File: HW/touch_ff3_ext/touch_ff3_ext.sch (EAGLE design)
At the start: 6 parts, among them M1 SMALL_SERVO, P8 DF9-31P, Q1 MOSFET-NCHANNELAO3404A, X3 DF9-31S

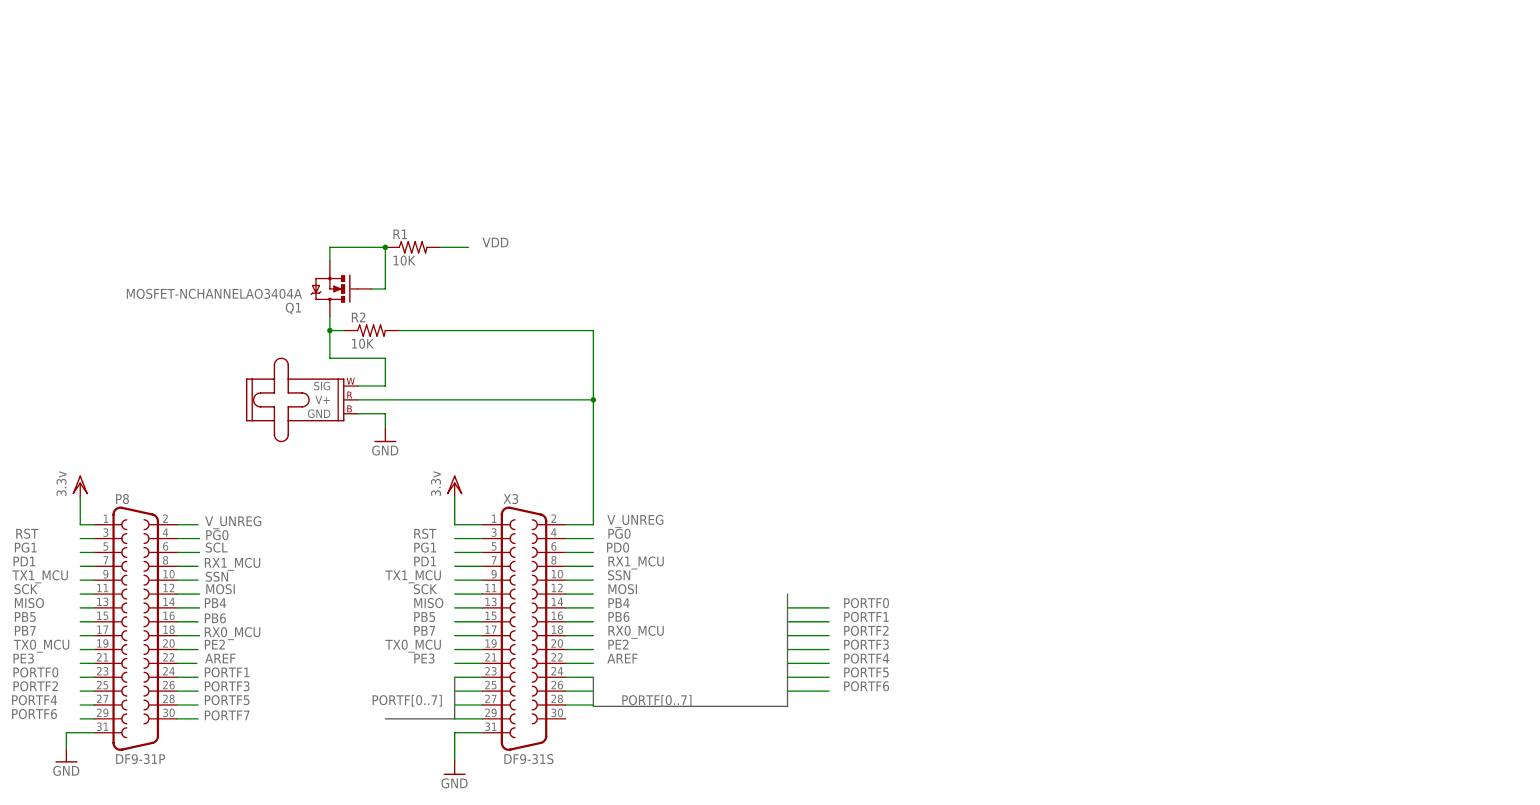
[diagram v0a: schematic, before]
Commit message: updated pcb, removed .swp file from fw dir
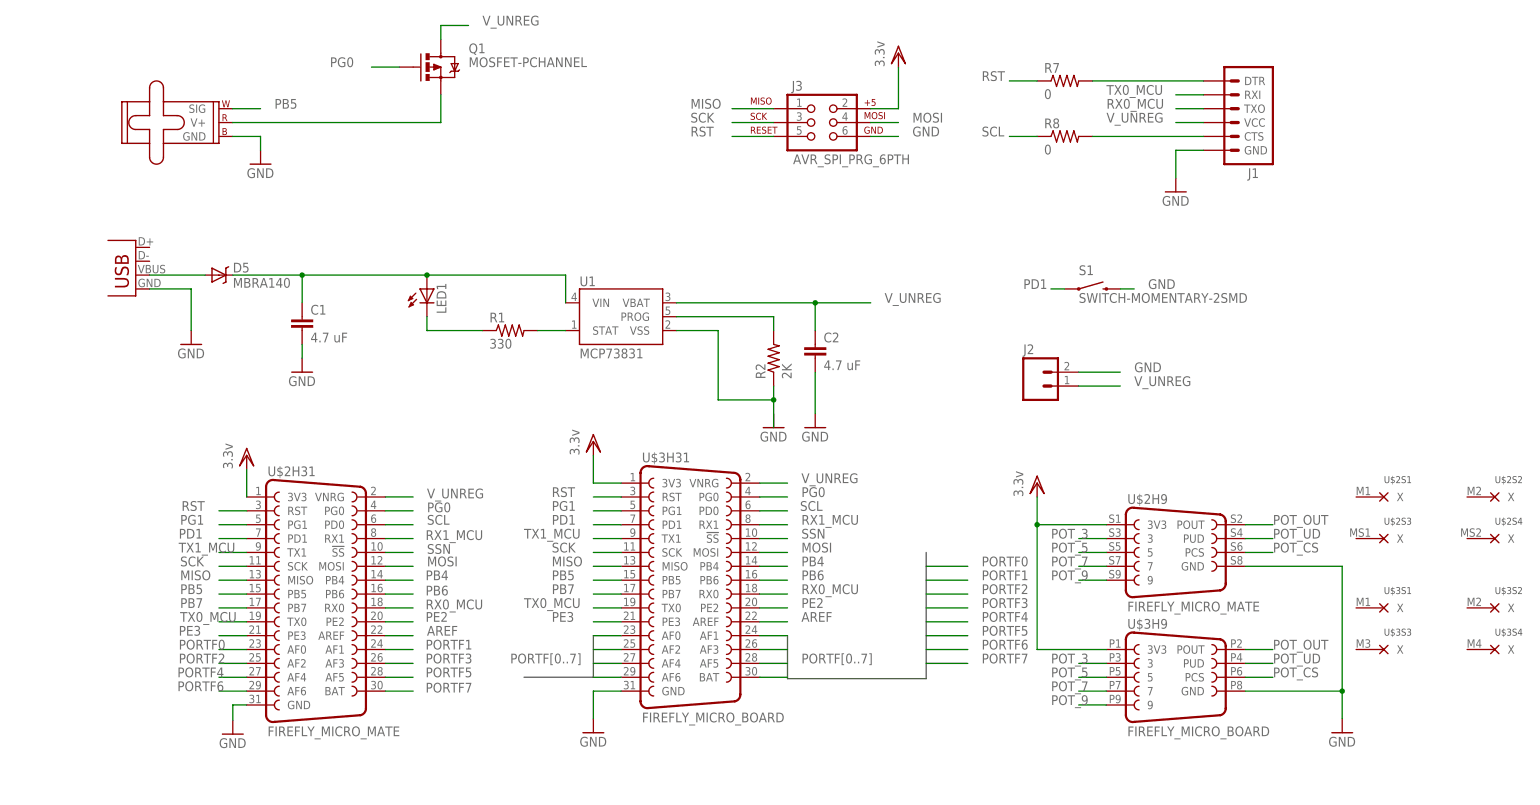
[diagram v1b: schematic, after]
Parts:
- removed P8: DF9-31P, con-hirose:DF9-31P
- removed X3: DF9-31S, con-hirose:DF9-31S
- added C1, C2: 4.7 uF, SparkFun-Capacitors:CAP1206
- added D5: MBRA140, SparkFun-DiscreteSemi:MBRA140
- added J1: (no value), SparkFun-Connectors:ARDUINO_SERIAL_PROGRAMPTH
- added J2: (no value), SparkFun-Connectors:M02PTH
- added J3: AVR_SPI_PRG_6PTH, SparkFun-Connectors:AVR_SPI_PRG_6PTH
- added LED1: (no value), LilyPad-Wearables:LED1206
- added R7, R8: 0, SparkFun-Passives:RESISTOR1206
- added S1: SWITCH-MOMENTARY-2SMD, SparkFun-Electromechanical:SWITCH-MOMENTARY-2SMD
- added U$2: FIREFLY_MICRO_MATE, Boards:FIREFLY_MICRO_MATE
- added U$3: FIREFLY_MICRO_BOARD, Boards:FIREFLY_MICRO_BOARD
- added U1: MCP73831, SparkFun-PowerIC:MCP73831
- added X1: USBSMD, SparkFun-Connectors:USBSMD
- Q1: value MOSFET-NCHANNELAO3404A -> MOSFET-PCHANNEL; device SparkFun-DiscreteSemi:MOSFET-NCHANNELAO3404A -> SparkFun-DiscreteSemi:MOSFET-PCHANNEL
- R1: value 10K -> 330; device SparkFun-Passives:RESISTOR1206 -> SparkFun-Resistors:RESISTOR1206
- R2: value 10K -> 2K; device SparkFun-Passives:RESISTOR1206 -> SparkFun-Resistors:RESISTOR1206
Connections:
- removed net HPB4: M1.SIG, Q1.D, R2.1
- removed net PD0: X3.6
- new net N$1: R2.1, U1.VSS
- new net N$10: D5.A, X1.VBUS
- new net N$17: R2.2, U1.PROG
- new net N$18: J1.DTR, R7.2
- new net N$19: J1.CTS, R8.2
- new net N$6: C1.1, D5.C, LED1.A, U1.VIN
- new net N$7: R1.2, U1.STAT
- new net N$9: LED1.C, R1.1
- new net POT_3: U$2H9.3, U$3H9.3
- new net POT_5: U$2H9.5, U$3H9.5
- new net POT_7: U$2H9.7, U$3H9.7
- new net POT_9: U$2H9.9, U$3H9.9
- new net POT_CS: U$2H9.PCS, U$3H9.PCS
- new net POT_OUT: U$2H9.POUT, U$3H9.POUT
- new net POT_UD: U$2H9.PUD, U$3H9.PUD
- net AREF: now also U$2H31.AREF, U$3H31.AREF; no longer P8.22, X3.22
- net GND: now also C1.2, C2.2, J1.GND, J2.2, J3.6, S1.2, U$2H31.GND, U$2H9.GND, U$3H31.GND, U$3H9.GND, X1.GND; no longer P8.31, X3.31
- net MISO: now also J3.1, U$2H31.MISO, U$3H31.MISO; no longer P8.13, X3.13
- net MOSI: now also J3.4, U$2H31.MOSI, U$3H31.MOSI; no longer P8.12, X3.12
- net N$2: now also M1.V+; no longer Q1.G, R1.1
- net PB4: now also U$2H31.PB4, U$3H31.PB4; no longer P8.14, X3.14
- net PB5: now also M1.SIG, U$2H31.PB5, U$3H31.PB5; no longer P8.15, X3.15
- net PB6: now also U$2H31.PB6, U$3H31.PB6; no longer P8.16, X3.16
- net PB7: now also U$2H31.PB7, U$3H31.PB7; no longer P8.17, X3.17
- net PD1: now also S1.1, U$2H31.PD1, U$3H31.PD1; no longer P8.7, X3.7
- net PE2: now also U$2H31.PE2, U$3H31.PE2; no longer P8.20, X3.20
- net PE3: now also U$2H31.PE3, U$3H31.PE3; no longer P8.21, X3.21
- net PG0: now also Q1.G, U$2H31.PG0, U$3H31.PG0; no longer P8.4, X3.4
- net PG1: now also U$2H31.PG1, U$3H31.PG1; no longer P8.5, X3.5
- net PORTF0: now also U$2H31.AF0, U$3H31.AF0; no longer P8.23, X3.23
- net PORTF1: now also U$2H31.AF1, U$3H31.AF1; no longer P8.24, X3.24
- net PORTF2: now also U$2H31.AF2, U$3H31.AF2; no longer P8.25, X3.25
- net PORTF3: now also U$2H31.AF3, U$3H31.AF3; no longer P8.26, X3.26
- net PORTF4: now also U$2H31.AF4, U$3H31.AF4; no longer P8.27, X3.27
- net PORTF5: now also U$2H31.AF5, U$3H31.AF5; no longer P8.28, X3.28
- net PORTF6: now also U$2H31.AF6, U$3H31.AF6; no longer P8.29, X3.29
- net PORTF7: now also U$2H31.BAT, U$3H31.BAT; no longer P8.30
- net RST: now also J3.5, R7.1, U$2H31.RST, U$3H31.RST; no longer P8.3, X3.3
- net RX0_MCU: now also J1.TXO, U$2H31.RX0, U$3H31.RX0; no longer P8.18, X3.18
- net RX1_MCU: now also U$2H31.RX1, U$3H31.RX1; no longer P8.8, X3.8
- net SCK: now also J3.3, U$2H31.SCK, U$3H31.SCK; no longer P8.11, X3.11
- net SCL: now also R8.1, U$2H31.PD0, U$3H31.PD0; no longer P8.6
- net SSN: now also U$2H31.!SS, U$3H31.!SS; no longer P8.10, X3.10
- net TX0_MCU: now also J1.RXI, U$2H31.TX0, U$3H31.TX0; no longer P8.19, X3.19
- net TX1_MCU: now also U$2H31.TX1, U$3H31.TX1; no longer P8.9, X3.9
- net VDD: now also J3.2, U$2H31.3V3, U$2H9.3V3, U$3H31.3V3, U$3H9.3V3; no longer P8.1, R1.2, X3.1
- net V_UNREG: now also C2.1, J1.VCC, J2.1, Q1.D, U$2H31.VNRG, U$3H31.VNRG, U1.VBAT; no longer M1.V+, P8.2, R2.2, X3.2
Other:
- moved on the sheet: Q1, R1, R2

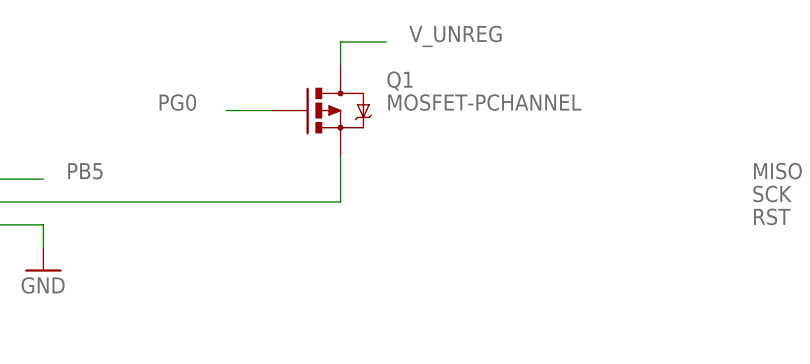
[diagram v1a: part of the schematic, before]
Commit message: updated transistor, routed 1 last connection, added vias to balance out gnd planes
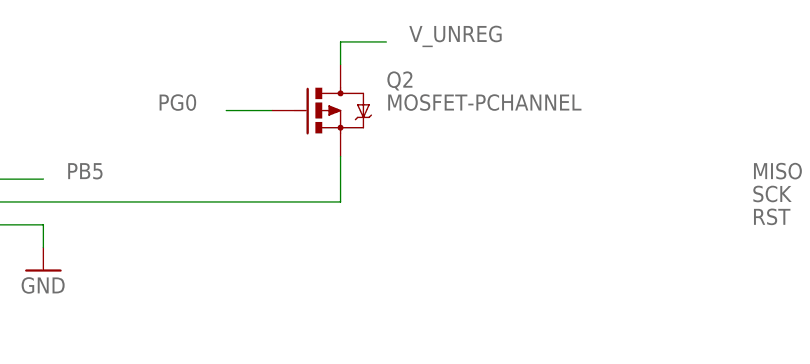
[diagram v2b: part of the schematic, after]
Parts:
- renumbered Q1 to Q2
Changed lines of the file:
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@@
 <part name="R1" library="SparkFun-Resistors" deviceset="RESISTOR" device="1206" value="330"/>
 <part name="R2" library="SparkFun-Resistors" deviceset="RESISTOR" device="1206" value="2K"/>
-<part name="Q1" library="SparkFun-DiscreteSemi" deviceset="MOSFET-PCHANNEL" device=""/>
+<part name="Q2" library="SparkFun-DiscreteSemi" deviceset="MOSFET-PCHANNEL" device=""/>
 </parts>
 <sheets>
@@
 <instance part="R1" gate="G$1" x="127" y="96.52"/>
 <instance part="R2" gate="G$1" x="175.26" y="91.44" rot="R90"/>
-<instance part="Q1" gate="G$1" x="114.3" y="144.78"/>
+<instance part="Q2" gate="G$1" x="114.3" y="144.78"/>
 </instances>
 <busses>
@@
 </segment>
 <segment>
-<pinref part="Q1" gate="G$1" pin="D"/>
 <wire x1="114.3" y1="149.86" x2="114.3" y2="152.4" width="0.1524" layer="91"/>
 <wire x1="114.3" y1="152.4" x2="119.38" y2="152.4" width="0.1524" layer="91"/>
 <label x="121.92" y="152.4" size="1.778" layer="95"/>
+<pinref part="Q2" gate="G$1" pin="D"/>
 </segment>
 </net>
@@
 </segment>
 <segment>
-<pinref part="Q1" gate="G$1" pin="G"/>
 <wire x1="106.68" y1="144.78" x2="101.6" y2="144.78" width="0.1524" layer="91"/>
 <label x="93.98" y="144.78" size="1.778" layer="95"/>
+<pinref part="Q2" gate="G$1" pin="G"/>
 </segment>
 </net>
@@
 <net name="N$2" class="0">
 <segment>
-<pinref part="Q1" gate="G$1" pin="S"/>
 <wire x1="114.3" y1="139.7" x2="114.3" y2="134.62" width="0.1524" layer="91"/>
 <pinref part="M1" gate="G$1" pin="V+"/>
 <wire x1="114.3" y1="134.62" x2="76.2" y2="134.62" width="0.1524" layer="91"/>
-</segment>
-</net>
+<pinref part="Q2" gate="G$1" pin="S"/>
+</segment>
+</net>

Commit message: updated pcb, added servo on off code
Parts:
- removed J1: (no value), SparkFun-Connectors:ARDUINO_SERIAL_PROGRAMPTH
- removed Q2: MOSFET-PCHANNEL, SparkFun-DiscreteSemi:MOSFET-PCHANNEL
- removed R7, R8: 0, SparkFun-Passives:RESISTOR1206
- removed S1: SWITCH-MOMENTARY-2SMD, SparkFun-Electromechanical:SWITCH-MOMENTARY-2SMD
- added Q1: MOSFET-NCHANNELBSS123LT1G, SparkFun-DiscreteSemi:MOSFET-NCHANNELBSS123LT1G
- added R3: 100, SparkFun-Passives:RESISTOR1206
- added R4: 1k, SparkFun-Passives:RESISTOR1206
- added S2: (no value), SparkFun-Electromechanical:SWITCH-SPDT-SMD-A
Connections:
- removed net N$1: R2.1, U1.VSS
- removed net N$18: J1.DTR, R7.2
- removed net N$19: J1.CTS, R8.2
- new net N$3: Q1.G, R3.2, R4.2
- new net V_BAT: C2.1, J2.1, S2.P, U1.VBAT
- net GND: now also Q1.S, R2.1, R4.1, U1.VSS; no longer J1.GND, M1.GND, S1.2
- net N$2: now also M1.GND, Q1.D; no longer M1.V+, Q2.S
- net PD1: no longer S1.1
- net PG0: now also R3.1; no longer Q2.G
- net RST: no longer R7.1
- net RX0_MCU: no longer J1.TXO
- net SCL: no longer R8.1
- net TX0_MCU: no longer J1.RXI
- net V_UNREG: now also M1.V+, S2.S; no longer C2.1, J1.VCC, J2.1, Q2.D, U1.VBAT
